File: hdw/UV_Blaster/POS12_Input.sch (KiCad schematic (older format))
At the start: 26 parts

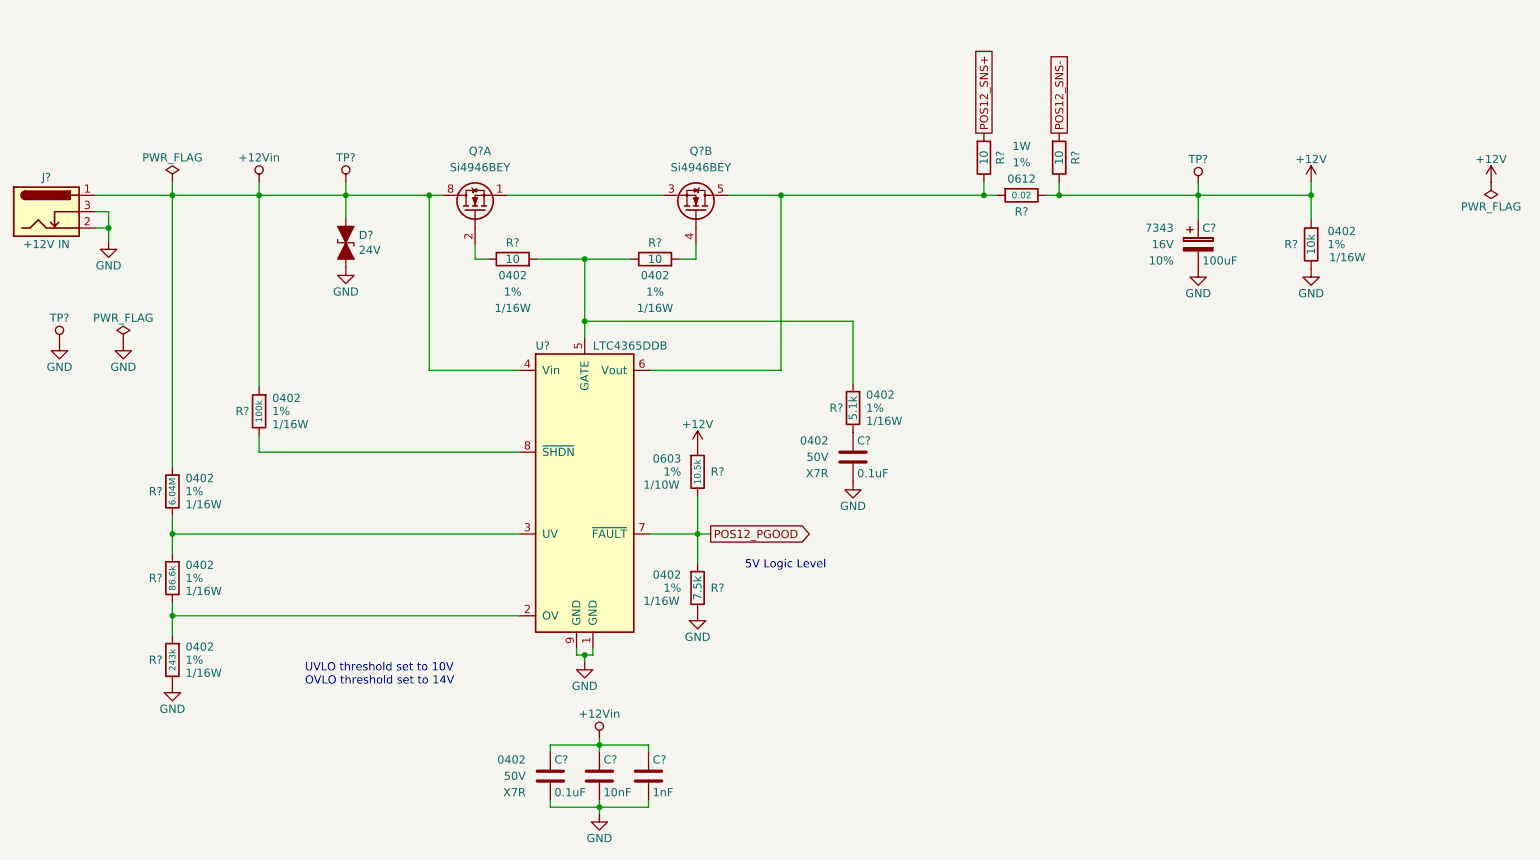
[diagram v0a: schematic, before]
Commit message: More sch work, netlist, part numbers, footprints
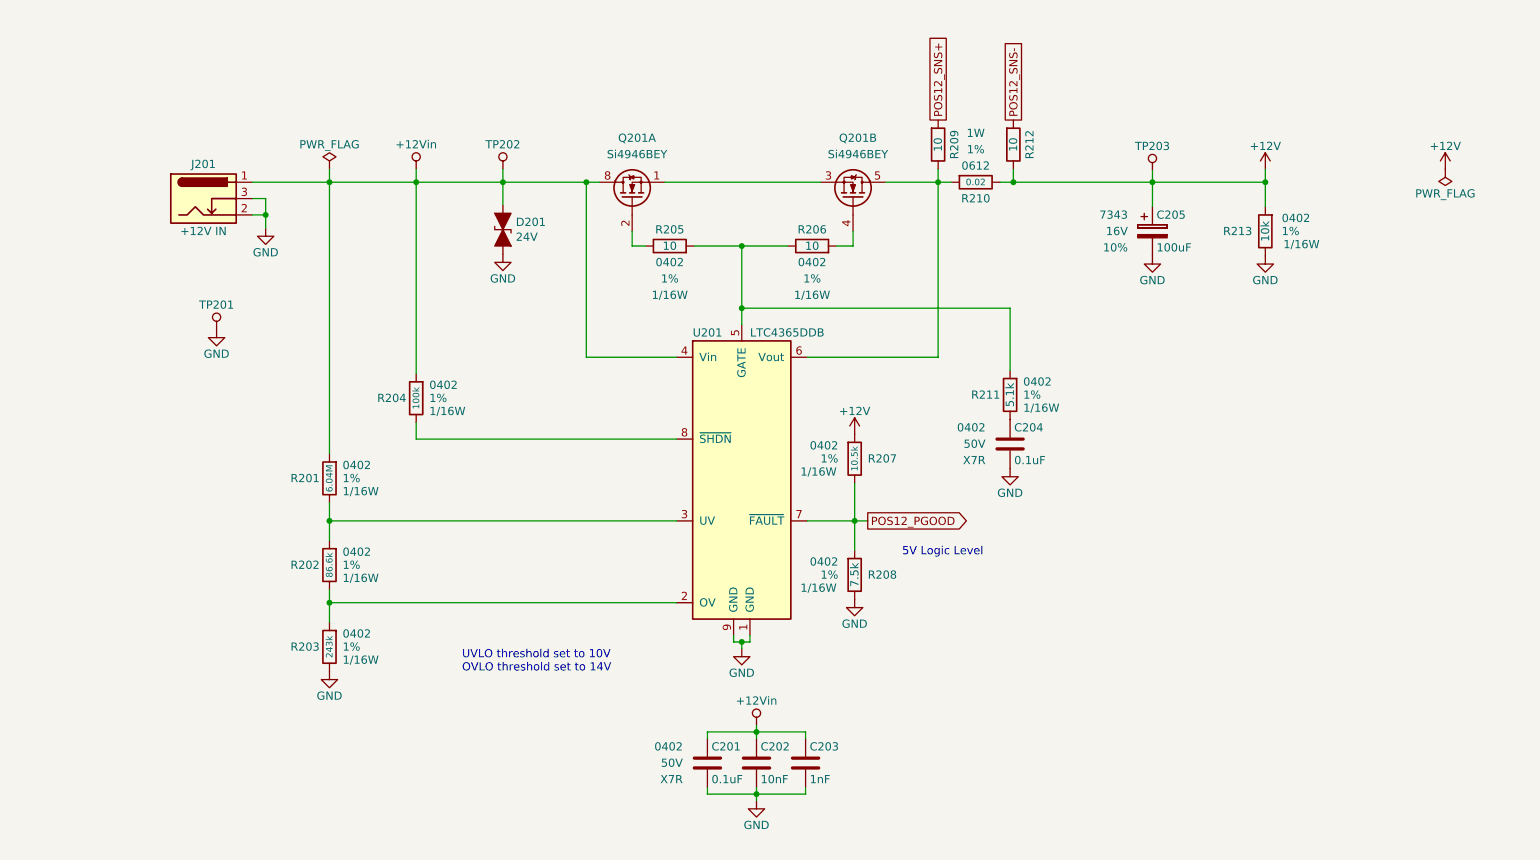
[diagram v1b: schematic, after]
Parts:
- J201: renamed from J?; Digi-Key PN CP-202BH-ND -> (none)
- R201: renamed from R?; Digi-Key PN (none) -> 541-CRCW04026M04FKEDCT-ND
- R202: renamed from R?; Digi-Key PN (none) -> P86.6KLCT-ND; Flow_Control (none) -> P86.6KLCT-ND
- R203: renamed from R?; Digi-Key PN (none) -> YAG3070CT-ND
- R204: renamed from R?; Digi-Key PN (none) -> 311-100KLRCT-ND
- R205, R206: renamed from R?; Digi-Key PN (none) -> 311-10.0LRCT-ND
- R207: renamed from R?; footprint Resistors_SMD:R_0603 -> Resistors_SMD:R_0402; Digi-Key PN 311-10.5KHRCT-ND -> RMCF0402FT10K5CT-ND; Wattage 1/10W -> 1/16W; display_footprint 0603 -> 0402
- R208: renamed from R?; footprint (none) -> Resistors_SMD:R_0402; Digi-Key PN (none) -> RMCF0402FT7K50CT-ND
- R209, R212: renamed from R?; Configuration (none) -> Telemetry; Digi-Key PN (none) -> 311-10.0LRCT-ND
- R211: renamed from R?; Digi-Key PN (none) -> P5.10KLCT-ND
- R213: renamed from R?; Digi-Key PN (none) -> 541-3959-1-ND
- gave numbers to parts that had none: 12
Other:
- moved on the sheet: C201, C202, C203, C204, C205, D201, J201, Q201A, Q201B, R201, R202, R203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
